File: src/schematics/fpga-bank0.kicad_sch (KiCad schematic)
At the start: 7 parts, among them U6 LFE5U-85F-*BG756*

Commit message: Add remaining component footprints (#79)
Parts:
- C48, C49, C50, C51, C52, C53: footprint (none) -> Capacitor_SMD:C_0402_1005Metric
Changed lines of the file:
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@@
 			)
 		)
-		(property "Footprint" ""
+		(property "Footprint" "Capacitor_SMD:C_0402_1005Metric"
 			(at 105.41 35.56 0)
 			(effects
@@
 			)
 		)
-		(property "Footprint" ""
+		(property "Footprint" "Capacitor_SMD:C_0402_1005Metric"
 			(at 135.89 35.56 0)
 			(effects
@@
 			)
 		)
-		(property "Footprint" ""
+		(property "Footprint" "Capacitor_SMD:C_0402_1005Metric"
 			(at 146.05 35.56 0)
 			(effects
@@
 			)
 		)
-		(property "Footprint" ""
+		(property "Footprint" "Capacitor_SMD:C_0402_1005Metric"
 			(at 125.73 35.56 0)
 			(effects
@@
 			)
 		)
-		(property "Footprint" ""
+		(property "Footprint" "Capacitor_SMD:C_0402_1005Metric"
 			(at 157.48 35.56 0)
 			(effects
@@
 			)
 		)
-		(property "Footprint" ""
+		(property "Footprint" "Capacitor_SMD:C_0402_1005Metric"
 			(at 115.57 35.56 0)
 			(effects

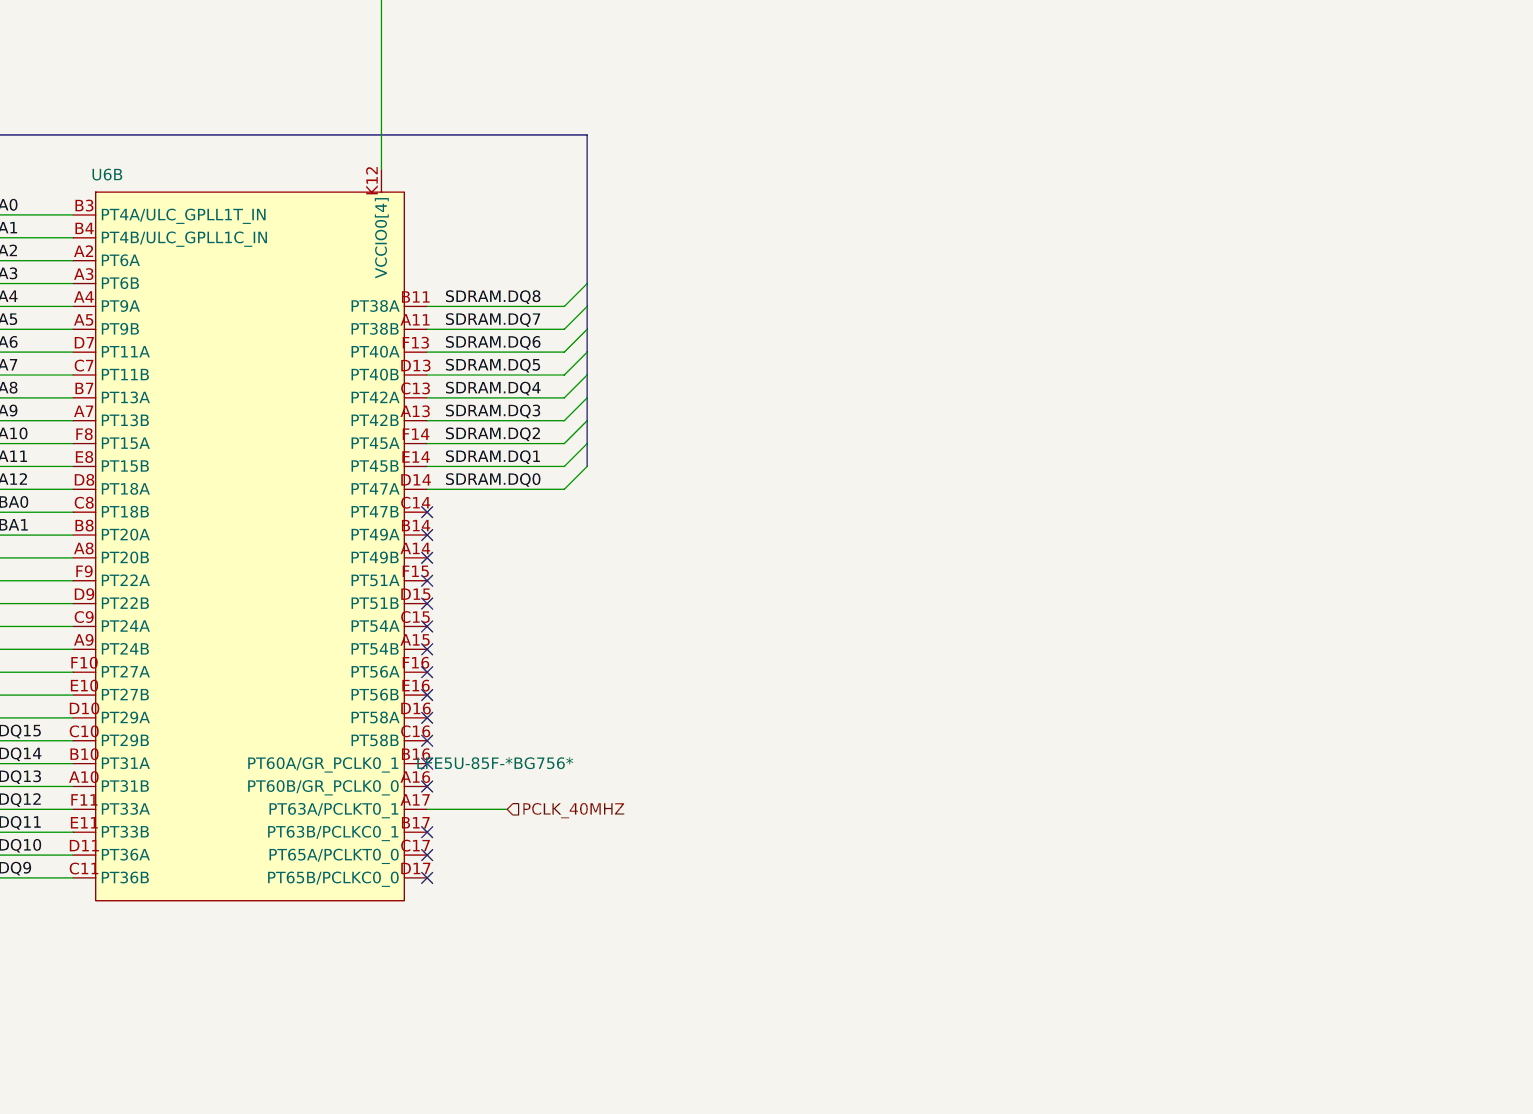
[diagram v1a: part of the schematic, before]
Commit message: Add notes on the schematic
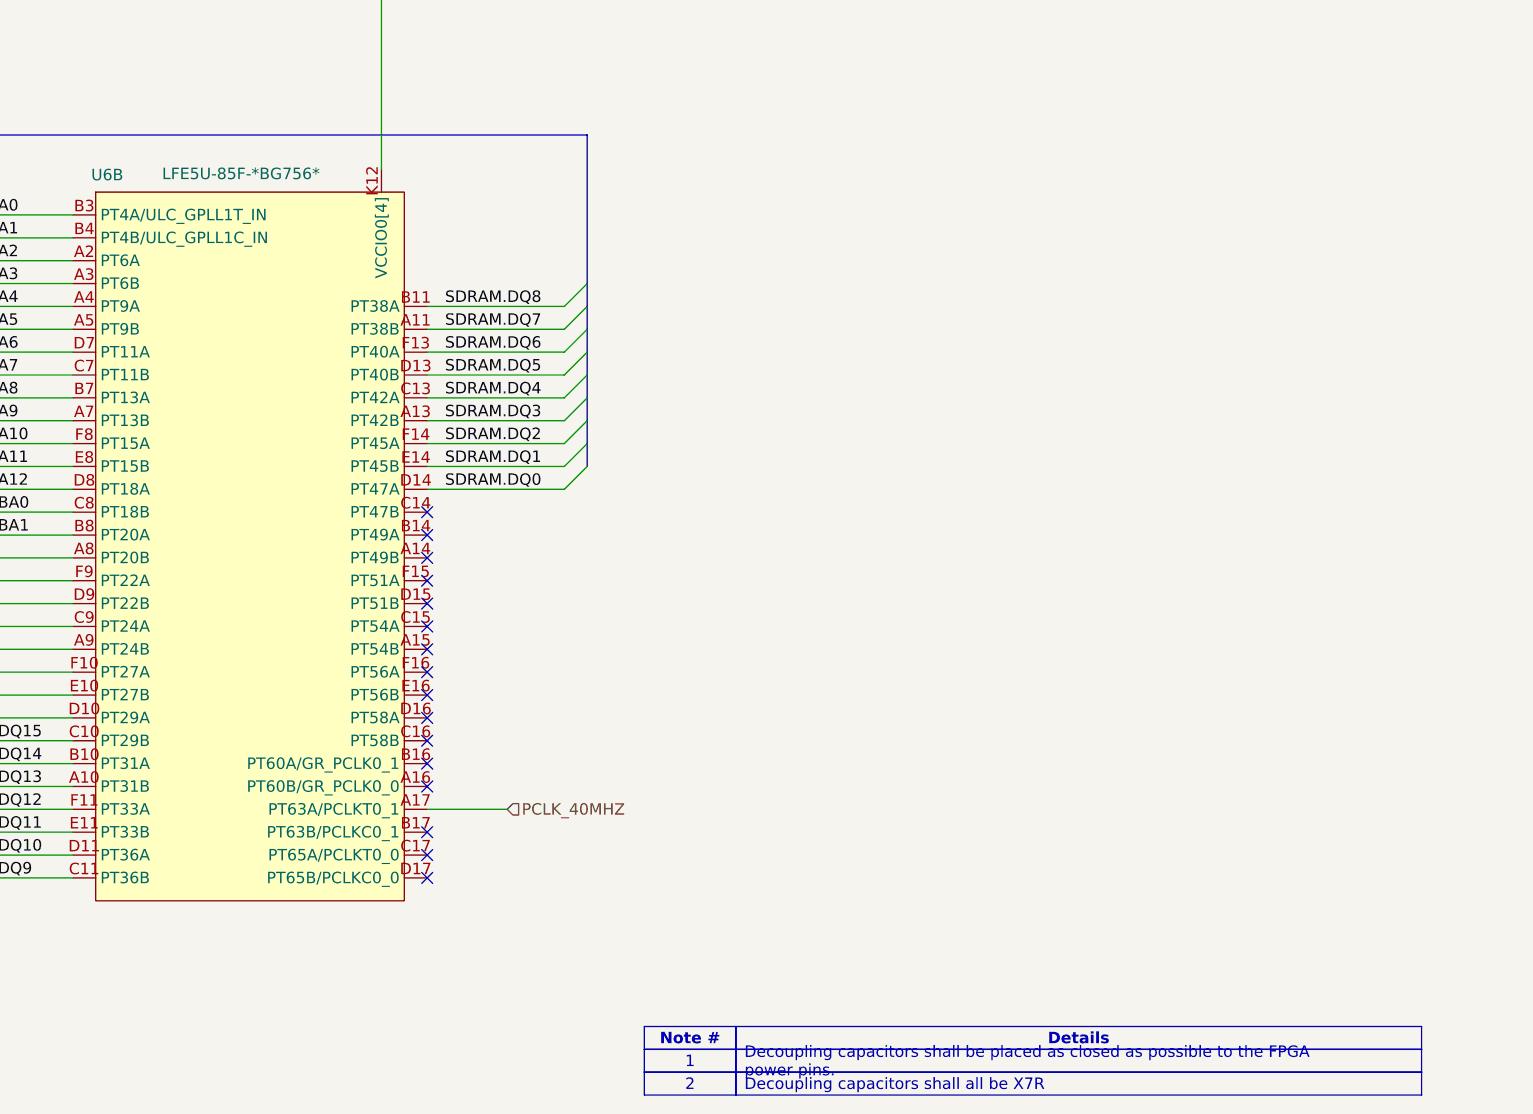
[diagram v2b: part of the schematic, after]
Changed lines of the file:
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@@
 		(comment 3 "${Part Number}")
+	)
+	(text_box "Note #"
+		(exclude_from_sim no)
+		(at 193.04 162.56 0)
+		(size 10.16 2.54)
+		(margins 0.9525 0.9525 0.9525 0.9525)
+		(stroke
+			(width 0)
+			(type solid)
+			(color 0 0 0 1)
+		)
+		(fill
+			(type none)
+		)
+		(effects
+			(font
+				(face "Arial")
+				(size 1.27 1.27)
+				(bold yes)
+				(color 0 0 0 1)
+			)
+		)
+	)
+	(text_box "Details"
+		(exclude_from_sim no)
+		(at 203.2 162.56 0)
+		(size 76.2 2.54)
+		(margins 0.9525 0.9525 0.9525 0.9525)
+		(stroke
+			(width 0)
+			(type solid)
+			(color 0 0 0 1)
+		)
+		(fill
+			(type none)
+		)
+		(effects
+			(font
+				(face "Arial")
+				(size 1.27 1.27)
+				(bold yes)
+				(color 0 0 0 1)
+			)
+		)
+	)
+	(text_box "Decoupling capacitors shall be placed as closed as possible to the FPGA power pins."
+		(exclude_from_sim no)
+		(at 203.2 165.1 0)
+		(size 76.2 2.54)
+		(margins 0.9525 0.9525 0.9525 0.9525)
+		(stroke
+			(width 0)
+			(type solid)
+			(color 0 0 0 1)
+		)
+		(fill
+			(type none)
+		)
+		(effects
+			(font
+				(face "Arial")
+				(size 1.27 1.27)
+				(color 0 0 0 1)
+			)
+			(justify left)
+		)
+	)
+	(text_box "Decoupling capacitors shall all be X7R"
+		(exclude_from_sim no)
+		(at 203.2 167.64 0)
+		(size 76.2 2.54)
+		(margins 0.9525 0.9525 0.9525 0.9525)
+		(stroke
+			(width 0)
+			(type solid)
+			(color 0 0 0 1)
+		)
+		(fill
+			(type none)
+		)
+		(effects
+			(font
+				(face "Arial")
+				(size 1.27 1.27)
+				(color 0 0 0 1)
+			)
+			(justify left)
+		)
+	)
+	(text_box "1"
+		(exclude_from_sim no)
+		(at 193.04 165.1 0)
+		(size 10.16 2.54)
+		(margins 0.9525 0.9525 0.9525 0.9525)
+		(stroke
+			(width 0)
+			(type solid)
+			(color 0 0 0 1)
+		)
+		(fill
+			(type none)
+		)
+		(effects
+			(font
+				(face "Arial")
+				(size 1.27 1.27)
+				(color 0 0 0 1)
+			)
+		)
+	)
+	(text_box "2"
+		(exclude_from_sim no)
+		(at 193.04 167.64 0)
+		(size 10.16 2.54)
+		(margins 0.9525 0.9525 0.9525 0.9525)
+		(stroke
+			(width 0)
+			(type solid)
+			(color 0 0 0 1)
+		)
+		(fill
+			(type none)
+		)
+		(effects
+			(font
+				(face "Arial")
+				(size 1.27 1.27)
+				(color 0 0 0 1)
+			)
+		)
 	)
 	(junction
@@
 		)
 		(property "Value" "LFE5U-85F-*BG756*"
-			(at 167.64 133.35 0)
-			(effects
-				(font
+			(at 139.446 67.818 0)
+			(effects
+				(font

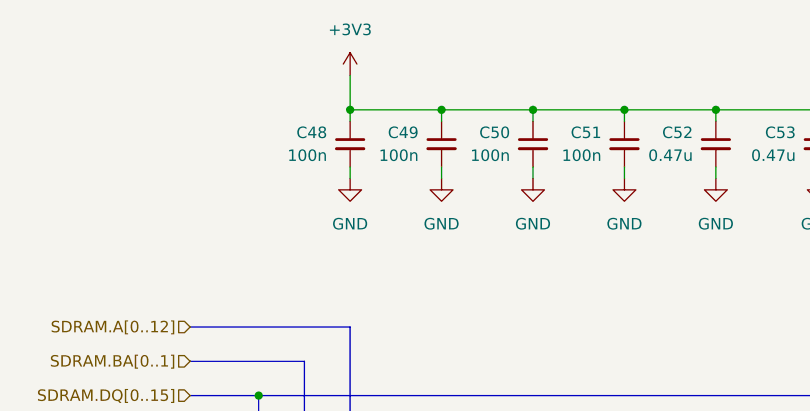
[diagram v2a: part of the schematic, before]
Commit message: Adds decoupling capacitors
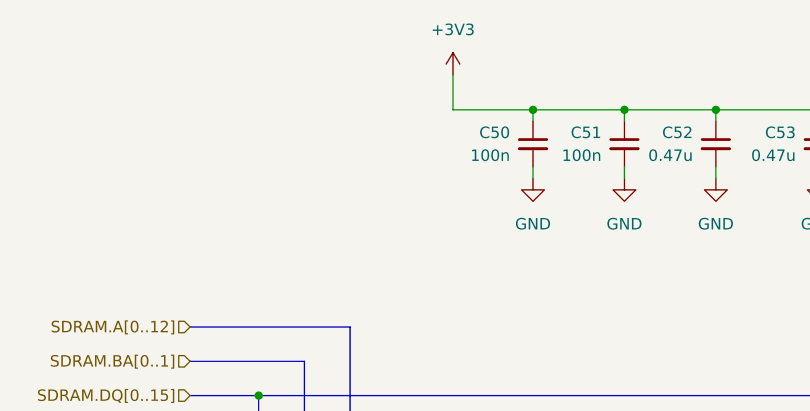
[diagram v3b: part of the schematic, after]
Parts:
- removed C48, C49: 100n, Capacitor_SMD:C_0402_1005Metric, symbol Device:C_Small
- C50, C51, C52, C53: footprint Capacitor_SMD:C_0402_1005Metric -> Capacitor_SMD:C_0201_0603Metric

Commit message: Route the SDRAM
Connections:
- net SDRAM.~{CS} is gone; now on net SDRAM.~{CAS}: U6.D9 (PT22B)
- net PCLK_40MHZ: no longer U6.A17 (PT63A/PCLKT0_1)
- net SDRAM.A0: now also U6.C10 (PT29B); no longer U6.B3 (PT4A/ULC_GPLL1T_IN)
- net SDRAM.A1: now also U6.C7 (PT11B); no longer U6.B4 (PT4B/ULC_GPLL1C_IN)
- net SDRAM.A10: now also U6.B3 (PT4A/ULC_GPLL1T_IN); no longer U6.F8 (PT15A)
- net SDRAM.A11: now also U6.C13 (PT42A); no longer U6.E8 (PT15B)
- net SDRAM.A12: now also U6.C14 (PT47B); no longer U6.D8 (PT18A)
- net SDRAM.A2: now also U6.B4 (PT4B/ULC_GPLL1C_IN); no longer U6.A2 (PT6A)
- net SDRAM.A3: now also U6.B10 (PT31A); no longer U6.A3 (PT6B)
- net SDRAM.A4: now also U6.C17 (PT65A/PCLKT0_0); no longer U6.A4 (PT9A)
- net SDRAM.A5: now also U6.B16 (PT60A/GR_PCLK0_1); no longer U6.A5 (PT9B)
- net SDRAM.A6: now also U6.B14 (PT49A); no longer U6.D7 (PT11A)
- net SDRAM.A7: now also U6.C16 (PT58B); no longer U6.C7 (PT11B)
- net SDRAM.A8: now also U6.C15 (PT54A); no longer U6.B7 (PT13A)
- net SDRAM.A9: now also U6.C11 (PT36B); no longer U6.A7 (PT13B)
- net SDRAM.BA0: now also U6.C9 (PT24A); no longer U6.C8 (PT18B)
- net SDRAM.CKE: now also U6.D10 (PT29A); no longer U6.F9 (PT22A)
- net SDRAM.CLK: now also U6.D11 (PT36A); no longer U6.A8 (PT20B)
- net SDRAM.DQ0: now also U6.A7 (PT13B); no longer U6.D14 (PT47A)
- net SDRAM.DQ1: now also U6.A5 (PT9B); no longer U6.E14 (PT45B)
- net SDRAM.DQ10: now also U6.A16 (PT60B/GR_PCLK0_0); no longer U6.D11 (PT36A)
- net SDRAM.DQ11: now also U6.A11 (PT38B); no longer U6.E11 (PT33B)
- net SDRAM.DQ12: now also U6.A15 (PT54B); no longer U6.F11 (PT33A)
- net SDRAM.DQ13: now also U6.A13 (PT42B); no longer U6.A10 (PT31B)
- net SDRAM.DQ14: now also U6.A14 (PT49B); no longer U6.B10 (PT31A)
- net SDRAM.DQ15: now also U6.B11 (PT38A); no longer U6.C10 (PT29B)
- net SDRAM.DQ2: now also U6.B7 (PT13A); no longer U6.F14 (PT45A)
- net SDRAM.DQ3: now also U6.A4 (PT9A); no longer U6.A13 (PT42B)
- net SDRAM.DQ4: now also U6.A8 (PT20B); no longer U6.C13 (PT42A)
- net SDRAM.DQ5: now also U6.A3 (PT6B); no longer U6.D13 (PT40B)
- net SDRAM.DQ6: now also U6.A9 (PT24B); no longer U6.F13 (PT40A)
- net SDRAM.DQ7: now also U6.A2 (PT6A); no longer U6.A11 (PT38B)
- net SDRAM.DQ8: now also U6.A17 (PT63A/PCLKT0_1); no longer U6.B11 (PT38A)
- net SDRAM.DQ9: now also U6.A10 (PT31B); no longer U6.C11 (PT36B)
- net SDRAM.DQMH: now also U6.D14 (PT47A); no longer U6.D10 (PT29A)
- net SDRAM.DQML: now also U6.D7 (PT11A); no longer U6.E10 (PT27B)
- net SDRAM.~{CAS}: no longer U6.A9 (PT24B)
- net SDRAM.~{RAS}: now also U6.C8 (PT18B); no longer U6.F10 (PT27A)
- net SDRAM.~{WE}: now also U6.D8 (PT18A); no longer U6.C9 (PT24A)
- no-connect marks 16 -> 18

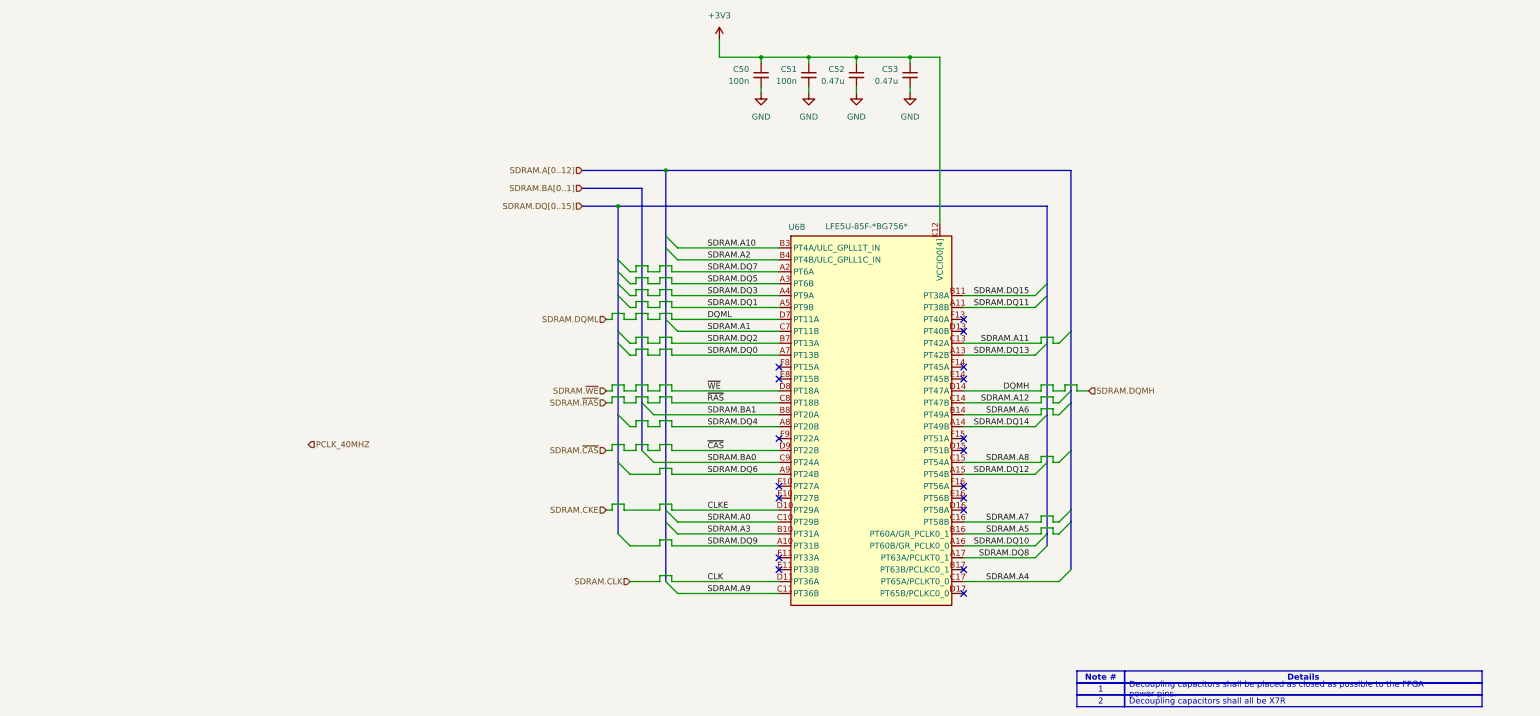
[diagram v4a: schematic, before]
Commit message: Add second SDRAM chip
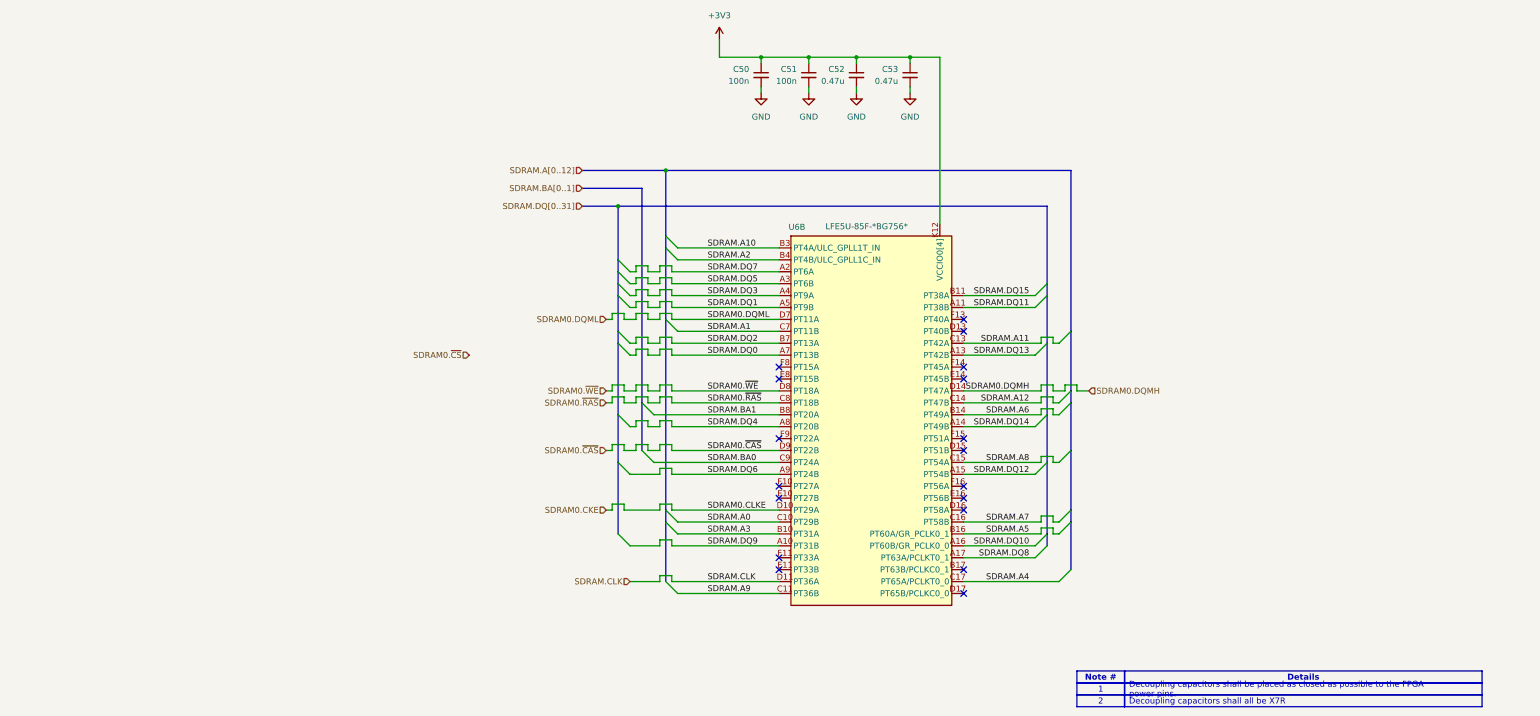
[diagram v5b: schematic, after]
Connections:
- net SDRAM.CKE renamed SDRAM0.CKE
- net SDRAM.DQMH renamed SDRAM0.DQMH
- net SDRAM.DQML renamed SDRAM0.DQML
- net SDRAM.~{CAS} renamed SDRAM0.~{CAS}
- net SDRAM.~{RAS} renamed SDRAM0.~{RAS}
- net SDRAM.~{WE} renamed SDRAM0.~{WE}
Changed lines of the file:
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@@
 		)
 	)
-	(label "DQMH"
+	(label "SDRAM0.DQMH"
 		(at 182.88 102.87 180)
 		(effects
@@
 		)
 	)
-	(label "~{RAS}"
+	(label "SDRAM0.~{RAS}"
 		(at 114.3 105.41 0)
 		(effects
@@
 		)
 	)
-	(label "CLK"
+	(label "SDRAM.CLK"
 		(at 114.3 143.51 0)
 		(effects
@@
 		)
 	)
-	(label "~{CAS}"
+	(label "SDRAM0.~{CAS}"
 		(at 114.3 115.57 0)
 		(effects
@@
 		)
 	)
-	(label "CLKE"
+	(label "SDRAM0.CLKE"
 		(at 114.3 128.27 0)
 		(effects
@@
 		)
 	)
-	(label "~{WE}"
+	(label "SDRAM0.~{WE}"
 		(at 114.3 102.87 0)
 		(effects
@@
 		)
 	)
-	(label "DQML"
+	(label "SDRAM0.DQML"
 		(at 114.3 87.63 0)
 		(effects
@@
 		)
 	)
+	(hierarchical_label "SDRAM0.~{CS}"
+		(shape input)
+		(at 63.5 95.25 180)
+		(effects
+			(font
+				(size 1.27 1.27)
+			)
+			(justify right)
+		)
+	)
 	(hierarchical_label "SDRAM.A[0..12]"
 		(shape input)
@@
 		)
 	)
-	(hierarchical_label "PCLK_40MHZ"
-		(shape input)
-		(at 29.21 114.3 0)
-		(effects
-			(font
-				(size 1.27 1.27)
-			)
-			(justify left)
-		)
-	)
-	(hierarchical_label "SDRAM.DQ[0..15]"
+	(hierarchical_label "SDRAM.DQ[0..31]"
 		(shape input)
 		(at 87.63 63.5 180)
@@
 		)
 	)
-	(hierarchical_label "SDRAM.~{WE}"
+	(hierarchical_label "SDRAM0.~{WE}"
 		(shape input)
 		(at 92.71 102.87 180)
@@
 		)
 	)
-	(hierarchical_label "SDRAM.~{RAS}"
+	(hierarchical_label "SDRAM0.~{RAS}"
 		(shape input)
 		(at 92.71 105.41 180)
@@
 		)
 	)
-	(hierarchical_label "SDRAM.~{CAS}"
+	(hierarchical_label "SDRAM0.~{CAS}"
 		(shape input)
 		(at 92.71 115.57 180)
@@
 		)
 	)
-	(hierarchical_label "SDRAM.DQML"
+	(hierarchical_label "SDRAM0.DQML"
 		(shape input)
 		(at 92.71 87.63 180)
@@
 		)
 	)
-	(hierarchical_label "SDRAM.CKE"
+	(hierarchical_label "SDRAM0.CKE"
 		(shape input)
 		(at 92.71 128.27 180)
@@
 		)
 	)
-	(hierarchical_label "SDRAM.DQMH"
+	(hierarchical_label "SDRAM0.DQMH"
 		(shape input)
 		(at 195.58 102.87 0)
